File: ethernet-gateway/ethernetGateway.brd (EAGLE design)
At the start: 50 x 50 mm, 57 parts, among them IC1 IC_ENC28J60-SOIC-28, IC2 REG1117, IC3 IC_FT230X-SSOP-16, J1 MAGJACK, J3 AVR_SPI_PRG_6PTH, U2 ATMEGA328P

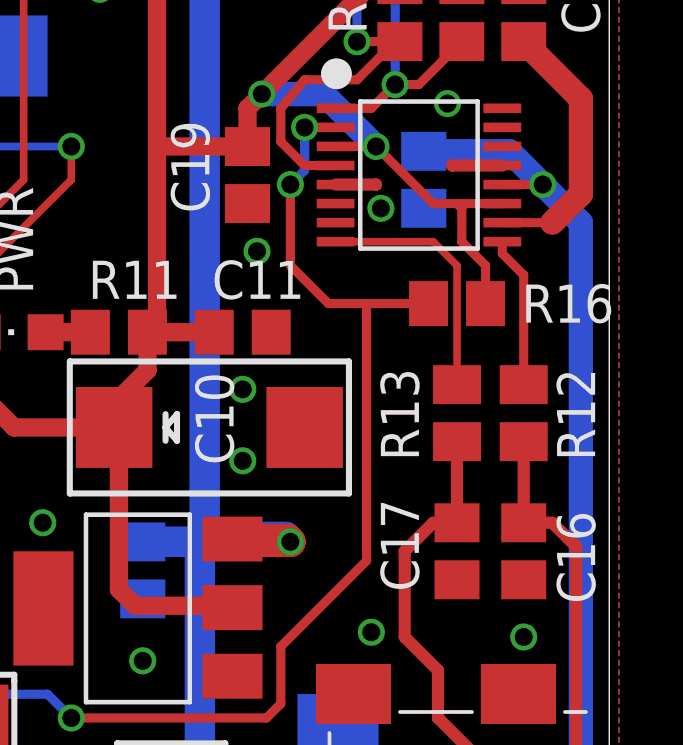
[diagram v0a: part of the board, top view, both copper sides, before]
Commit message: Update ethernet gateway reset circuit
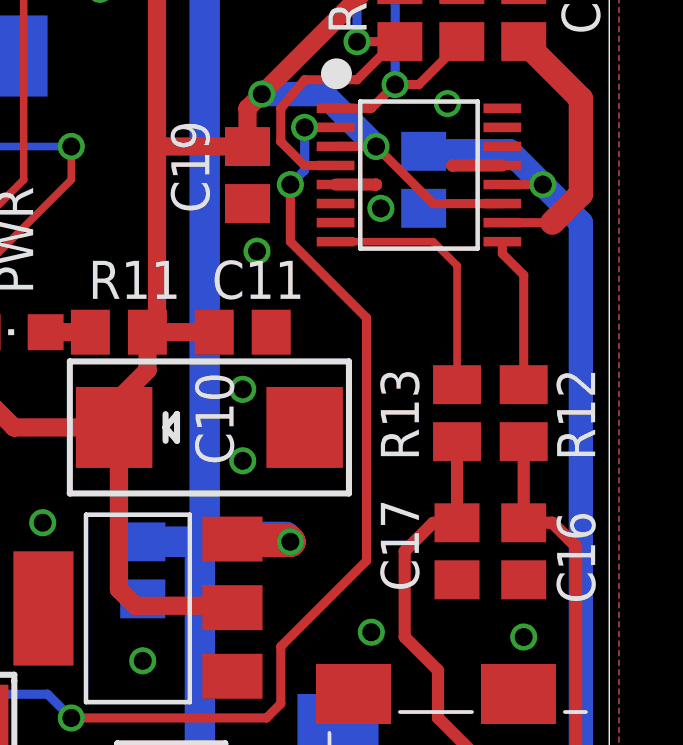
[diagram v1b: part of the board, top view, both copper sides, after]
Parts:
- removed R16: 10k, rcl:R0805
- R7: value 2k32 -> 6k8
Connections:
- net 3V3: no longer R16.1
- net N$20: no longer R16.2
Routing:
- net 3V3: track 155.8 -> 152.0 mm
- net N$20: track 38.1 -> 35.3 mm
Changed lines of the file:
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@@
 <attribute name="VALUE" x="33.3375" y="47.3075" size="1.27" layer="27" rot="R180"/>
 </element>
-<element name="R7" library="rcl" package="R0805" value="2k32" x="26.3525" y="18.415" smashed="yes" rot="MR180">
+<element name="R7" library="rcl" package="R0805" value="6k8" x="26.3525" y="18.415" smashed="yes" rot="MR180">
 <attribute name="NAME" x="30.48" y="17.78" size="1.27" layer="26" rot="MR0"/>
 <attribute name="VALUE" x="25.7175" y="20.955" size="1.27" layer="28" rot="MR180"/>
@@
 <attribute name="NAME" x="28.2575" y="16.66875" size="1.27" layer="26" rot="MR180"/>
 <attribute name="VALUE" x="25.0825" y="18.7325" size="1.27" layer="28" rot="MR180"/>
-</element>
-<element name="R16" library="rcl" package="R0805" value="10k" x="45.24375" y="29.21" smashed="yes" rot="R180">
-<attribute name="NAME" x="50.4825" y="29.845" size="1.27" layer="25" rot="R180"/>
-<attribute name="VALUE" x="45.87875" y="31.75" size="1.27" layer="27" rot="R180"/>
 </element>
 </elements>
@@
 <contactref element="R14" pad="1"/>
 <contactref element="R15" pad="1"/>
-<contactref element="R16" pad="1"/>
 <wire x1="41.19475" y1="34.44925" x2="42.5445" y2="34.44925" width="0.3048" layer="1"/>
 <wire x1="42.5445" y1="34.44925" x2="42.545" y2="34.44875" width="0.3048" layer="1"/>
 <wire x1="42.545" y1="34.44875" x2="44.45" y2="32.54375" width="0.3048" layer="1"/>
-<wire x1="44.45" y1="32.54375" x2="45.24375" y2="32.54375" width="0.3048" layer="1"/>
-<wire x1="45.24375" y1="32.54375" x2="46.75225" y2="32.54375" width="0.3048" layer="1"/>
+<wire x1="44.45" y1="32.54375" x2="46.75225" y2="32.54375" width="0.3048" layer="1"/>
 <wire x1="46.75225" y1="32.54375" x2="46.75275" y2="32.54425" width="0.3048" layer="1"/>
 <wire x1="45.4025" y1="39.84375" x2="43.33875" y2="39.84375" width="0.6096" layer="1"/>
@@
 <wire x1="42.545" y1="34.44875" x2="40.79875" y2="36.195" width="0.8128" layer="16"/>
 <wire x1="40.79875" y1="36.195" x2="38.735" y2="36.195" width="0.8128" layer="16"/>
-<wire x1="45.4025" y1="32.385" x2="45.24375" y2="32.54375" width="0.3048" layer="1"/>
-<wire x1="46.19375" y1="29.21" x2="46.19625" y2="29.2125" width="0.3048" layer="1"/>
-<wire x1="46.19625" y1="29.2125" x2="46.19625" y2="30.48" width="0.3048" layer="1"/>
-<wire x1="46.19625" y1="30.48" x2="45.4025" y2="31.27375" width="0.3048" layer="1"/>
-<wire x1="45.4025" y1="31.27375" x2="45.4025" y2="32.385" width="0.3048" layer="1"/>
 </signal>
 <signal name="LEDA">
@@
 <signal name="N$20">
 <contactref element="C18" pad="2"/>
-<contactref element="R16" pad="2"/>
-<wire x1="42.2275" y1="29.21" x2="42.2275" y2="20.6375" width="0.3048" layer="1"/>
+<wire x1="42.2275" y1="28.73375" x2="42.2275" y2="20.6375" width="0.3048" layer="1"/>
 <wire x1="42.2275" y1="20.6375" x2="39.37" y2="17.78" width="0.3048" layer="1"/>
 <wire x1="39.37" y1="17.78" x2="39.37" y2="15.875" width="0.3048" layer="1"/>
@@
 <wire x1="31.59125" y1="16.1925" x2="27.3025" y2="16.1925" width="0.3048" layer="16"/>
 <contactref element="IC3" pad="2"/>
-<wire x1="42.2275" y1="29.21" x2="44.29375" y2="29.21" width="0.3048" layer="1"/>
-<wire x1="42.2275" y1="29.21" x2="40.9575" y2="29.21" width="0.3048" layer="1"/>
-<wire x1="40.9575" y1="29.21" x2="39.6875" y2="30.48" width="0.3048" layer="1"/>
-<wire x1="39.6875" y1="30.48" x2="39.6875" y2="33.17875" width="0.3048" layer="1"/>
+<wire x1="42.2275" y1="28.73375" x2="39.6875" y2="31.27375" width="0.3048" layer="1"/>
+<wire x1="39.6875" y1="31.27375" x2="39.6875" y2="33.17875" width="0.3048" layer="1"/>
 <via x="39.6875" y="33.17875" extent="1-16" drill="0.6" shape="octagon"/>
 <wire x1="39.6875" y1="33.17875" x2="40.16375" y2="33.655" width="0.3048" layer="16"/>

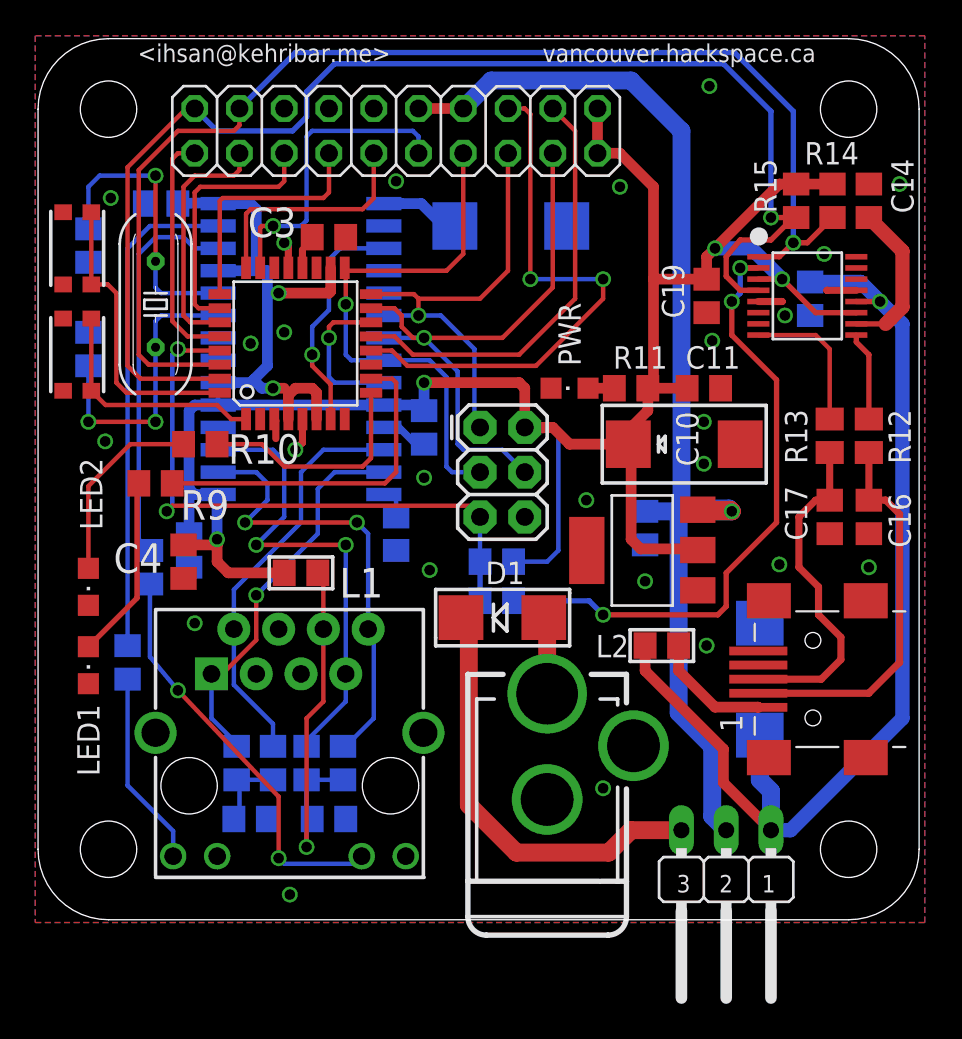
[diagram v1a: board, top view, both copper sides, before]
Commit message: Corrected errors in reset wiring
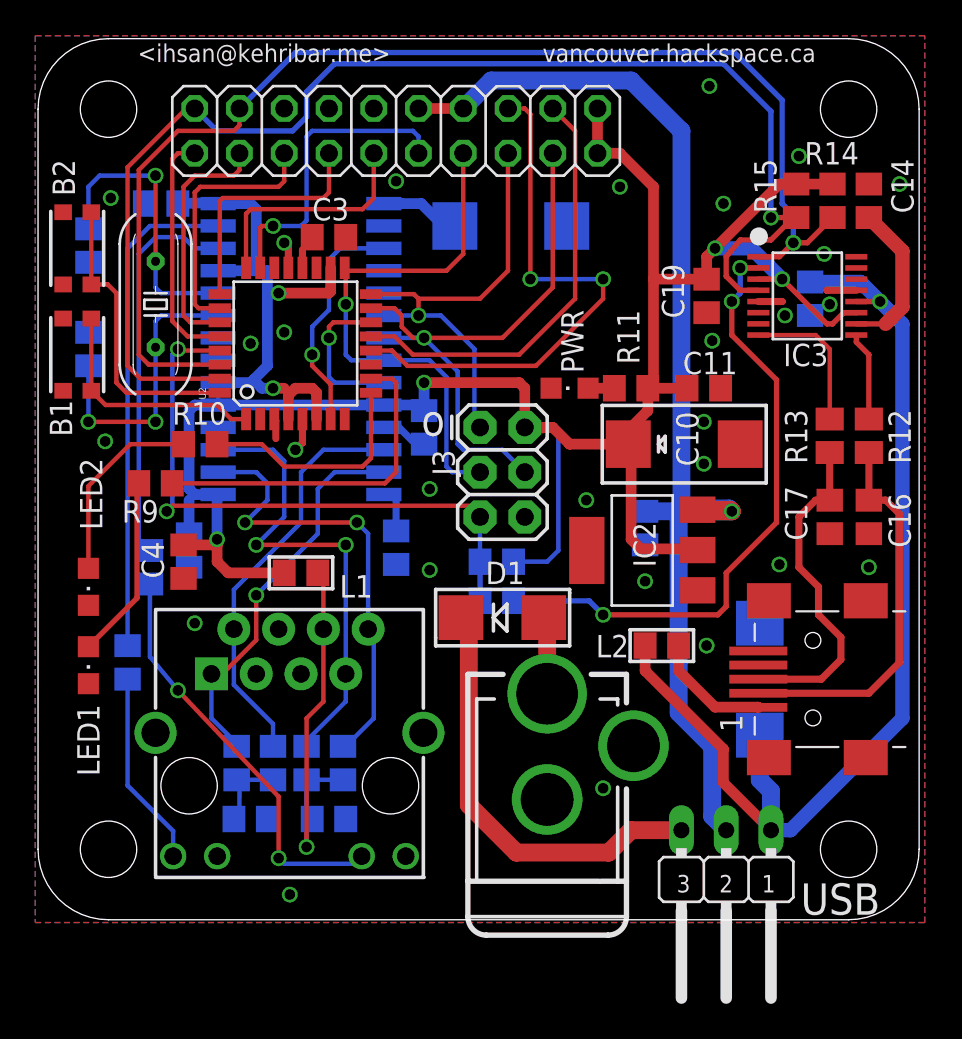
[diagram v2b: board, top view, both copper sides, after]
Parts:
- moved R8 0.79 mm to (20.6, 19.2)
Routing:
- net N$13: track 1.78 -> 2.58 mm
- net 3V3: track 152.0 -> 152.5 mm
- net GND: vias 25 -> 28
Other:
- board text added: "April 2014"
- board text added: "USB"
- board text added: "o"
- board text removed: "September 2013"
